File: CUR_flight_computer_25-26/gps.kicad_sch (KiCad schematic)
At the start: 4 parts, among them U1 SAM-M8Q

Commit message: update gps
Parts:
- removed C13: 1u, symbol Device:C_Small
- added 10k: R_Small_US, symbol Device:R_Small_US
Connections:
- net +3V3: now also 10k.2
- net ~{GPS_RES}: now also 10k.1
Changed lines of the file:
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@@
 	)
 	(junction
-		(at 149.86 86.36)
+		(at 120.65 114.3)
 		(diameter 0)
 		(color 0 0 0 0)
@@
 	(wire
 		(pts
-			(xy 142.24 86.36) (xy 149.86 86.36)
-		)
-		(stroke
-			(width 0)
-			(type default)
-		)
-	)
-	(wire
-		(pts
 			(xy 165.1 106.68) (xy 167.64 106.68)
 		)
@@
 	(wire
 		(pts
-			(xy 142.24 87.63) (xy 142.24 86.36)
-		)
-		(stroke
-			(width 0)
-			(type default)
-		)
-	)
-	(wire
-		(pts
 			(xy 172.72 104.14) (xy 177.8 104.14)
 		)
@@
 	(wire
 		(pts
+			(xy 120.65 102.87) (xy 120.65 105.41)
+		)
+		(stroke
+			(width 0)
+			(type default)
+		)
+	)
+	(wire
+		(pts
 			(xy 152.4 96.52) (xy 152.4 92.71)
 		)
@@
 	(wire
 		(pts
-			(xy 135.89 114.3) (xy 139.7 114.3)
+			(xy 116.84 114.3) (xy 120.65 114.3)
 		)
 		(stroke
@@
 	(wire
 		(pts
-			(xy 149.86 86.36) (xy 149.86 92.71)
-		)
-		(stroke
-			(width 0)
-			(type default)
-		)
-	)
-	(wire
-		(pts
 			(xy 172.72 106.68) (xy 177.8 106.68)
 		)
@@
 	(wire
 		(pts
+			(xy 120.65 114.3) (xy 139.7 114.3)
+		)
+		(stroke
+			(width 0)
+			(type default)
+		)
+	)
+	(wire
+		(pts
+			(xy 120.65 110.49) (xy 120.65 114.3)
+		)
+		(stroke
+			(width 0)
+			(type default)
+		)
+	)
+	(wire
+		(pts
 			(xy 152.4 92.71) (xy 149.86 92.71)
 		)
@@
 	(wire
 		(pts
-			(xy 149.86 83.82) (xy 149.86 86.36)
+			(xy 149.86 83.82) (xy 149.86 92.71)
 		)
 		(stroke
@@
 	(hierarchical_label "~{GPS_RES}"
 		(shape input)
-		(at 135.89 114.3 180)
+		(at 116.84 114.3 180)
 		(effects
 			(font
@@
 	)
 	(hierarchical_label "GPS_EXINT"
-		(shape input)
+		(shape output)
 		(at 135.89 106.68 180)
 		(effects
@@
 			)
 			(justify left)
+		)
+	)
+	(symbol
+		(lib_id "power:+3V3")
+		(at 120.65 102.87 0)
+		(unit 1)
+		(exclude_from_sim no)
+		(in_bom yes)
+		(on_board yes)
+		(dnp no)
+		(fields_autoplaced yes)
+		(property "Reference" "#PWR034"
+			(at 120.65 106.68 0)
+			(effects
+				(font
+					(size 1.27 1.27)
+				)
+				(hide yes)
+			)
+		)
+		(property "Value" "+3V3"
+			(at 120.65 97.79 0)
+			(effects
+				(font
+					(size 1.27 1.27)
+				)
+			)
+		)
+		(property "Footprint" ""
+			(at 120.65 102.87 0)
+			(effects
+				(font
+					(size 1.27 1.27)
+				)
+				(hide yes)
+			)
+		)
+		(property "Datasheet" ""
+			(at 120.65 102.87 0)
+			(effects
+				(font
+					(size 1.27 1.27)
+				)
+				(hide yes)
+			)
+		)
+		(property "Description" "Power symbol creates a global label with name \"+3V3\""
+			(at 120.65 102.87 0)
+			(effects
+				(font
+					(size 1.27 1.27)
+				)
+				(hide yes)
+			)
+		)
+		(pin "1"
+		)
+		(instances
+			(project ""
+				(path "/bf7761cc-1b32-4d86-809c-5f027005229b/e838d24c-cb75-4a46-b88f-e4466a269629"
+					(reference "#PWR034")
+					(unit 1)
+				)
+			)
 		)
 	)
@@
 	)
 	(symbol
-		(lib_id "power:GND")
-		(at 142.24 92.71 0)
-		(unit 1)
-		(exclude_from_sim no)
-		(in_bom yes)
-		(on_board yes)
-		(dnp no)
-		(fields_autoplaced yes)
-		(property "Reference" "#PWR013"
-			(at 142.24 99.06 0)
-			(effects
-				(font
-					(size 1.27 1.27)
-				)
-				(hide yes)
-			)
-		)
-		(property "Value" "GND"
-			(at 142.24 97.79 0)
-			(effects
-				(font
-					(size 1.27 1.27)
-				)
-			)
-		)
-		(property "Footprint" ""
-			(at 142.24 92.71 0)
-			(effects
-				(font
-					(size 1.27 1.27)
-				)
-				(hide yes)
-			)
-		)
-		(property "Datasheet" ""
-			(at 142.24 92.71 0)
-			(effects
-				(font
-					(size 1.27 1.27)
-				)
-				(hide yes)
-			)
-		)
-		(property "Description" "Power symbol creates a global label with name \"GND\" , ground"
-			(at 142.24 92.71 0)
-			(effects
-				(font
-					(size 1.27 1.27)
-				)
-				(hide yes)
-			)
-		)
-		(pin "1"
-		)
-		(instances
-			(project ""
-				(path "/bf7761cc-1b32-4d86-809c-5f027005229b/e838d24c-cb75-4a46-b88f-e4466a269629"
-					(reference "#PWR013")
-					(unit 1)
-				)
-			)
-		)
-	)
-	(symbol
 		(lib_id "Device:R_Small")
 		(at 170.18 104.14 90)
@@
 	)
 	(symbol
-		(lib_id "Device:C_Small")
-		(at 142.24 90.17 0)
-		(unit 1)
-		(exclude_from_sim no)
-		(in_bom yes)
-		(on_board yes)
-		(dnp no)
-		(fields_autoplaced yes)
-		(property "Reference" "C13"
-			(at 144.78 88.9062 0)
-			(effects
-				(font
-					(size 1.27 1.27)
-				)
-				(justify left)
-			)
-		)
-		(property "Value" "1u"
-			(at 144.78 91.4462 0)
-			(effects
-				(font
-					(size 1.27 1.27)
-				)
-				(justify left)
-			)
-		)
-		(property "Footprint" ""
-			(at 142.24 90.17 0)
-			(effects
-				(font
-					(size 1.27 1.27)
-				)
-				(hide yes)
-			)
-		)
-		(property "Datasheet" "~"
-			(at 142.24 90.17 0)
-			(effects
-				(font
-					(size 1.27 1.27)
-				)
-				(hide yes)
-			)
-		)
-		(property "Description" "Unpolarized capacitor, small symbol"
-			(at 142.24 90.17 0)
-			(effects
-				(font
-					(size 1.27 1.27)
-				)
-				(hide yes)
-			)
-		)
-		(pin "2"
-		)
-		(pin "1"
-		)
-		(instances
-			(project ""
-				(path "/bf7761cc-1b32-4d86-809c-5f027005229b/e838d24c-cb75-4a46-b88f-e4466a269629"
-					(reference "C13")
-					(unit 1)
-				)
-			)
-		)
-	)
-	(symbol
 		(lib_id "Device:R_Small")
 		(at 170.18 106.68 90)
@@
 					(unit 1)
 				)
+			)
+		)
+	)
+	(symbol
+		(lib_id "Device:R_Small_US")
+		(at 120.65 107.95 0)
+		(mirror x)
+		(unit 1)
+		(exclude_from_sim no)
+		(in_bom yes)
+		(on_board yes)
+		(dnp no)
+		(fields_autoplaced yes)
+		(property "Reference" "10k"
+			(at 118.11 106.6799 0)
+			(effects
+				(font
+					(size 1.27 1.27)
+				)
+				(justify right)
+			)
+		)
+		(property "Value" "R_Small_US"
+			(at 118.11 109.2199 0)
+			(effects
+				(font
+					(size 1.27 1.27)
+				)
+				(justify right)
+			)
+		)
+		(property "Footprint" ""
+			(at 120.65 107.95 0)
+			(effects
+				(font
+					(size 1.27 1.27)
+				)
+				(hide yes)
+			)
+		)
+		(property "Datasheet" "~"
+			(at 120.65 107.95 0)
+			(effects
+				(font
+					(size 1.27 1.27)
+				)
+				(hide yes)
+			)
+		)
+		(property "Description" "Resistor, small US symbol"
+			(at 120.65 107.95 0)
+			(effects
+				(font
+					(size 1.27 1.27)
+				)
+				(hide yes)
+			)
+		)
+		(pin "1"
+		)
+		(pin "2"
+		)
+		(instances
+			(project ""
+				(path "/bf7761cc-1b32-4d86-809c-5f027005229b/e838d24c-cb75-4a46-b88f-e4466a269629"
+					(reference "10k")
+					(unit 1)
+				)

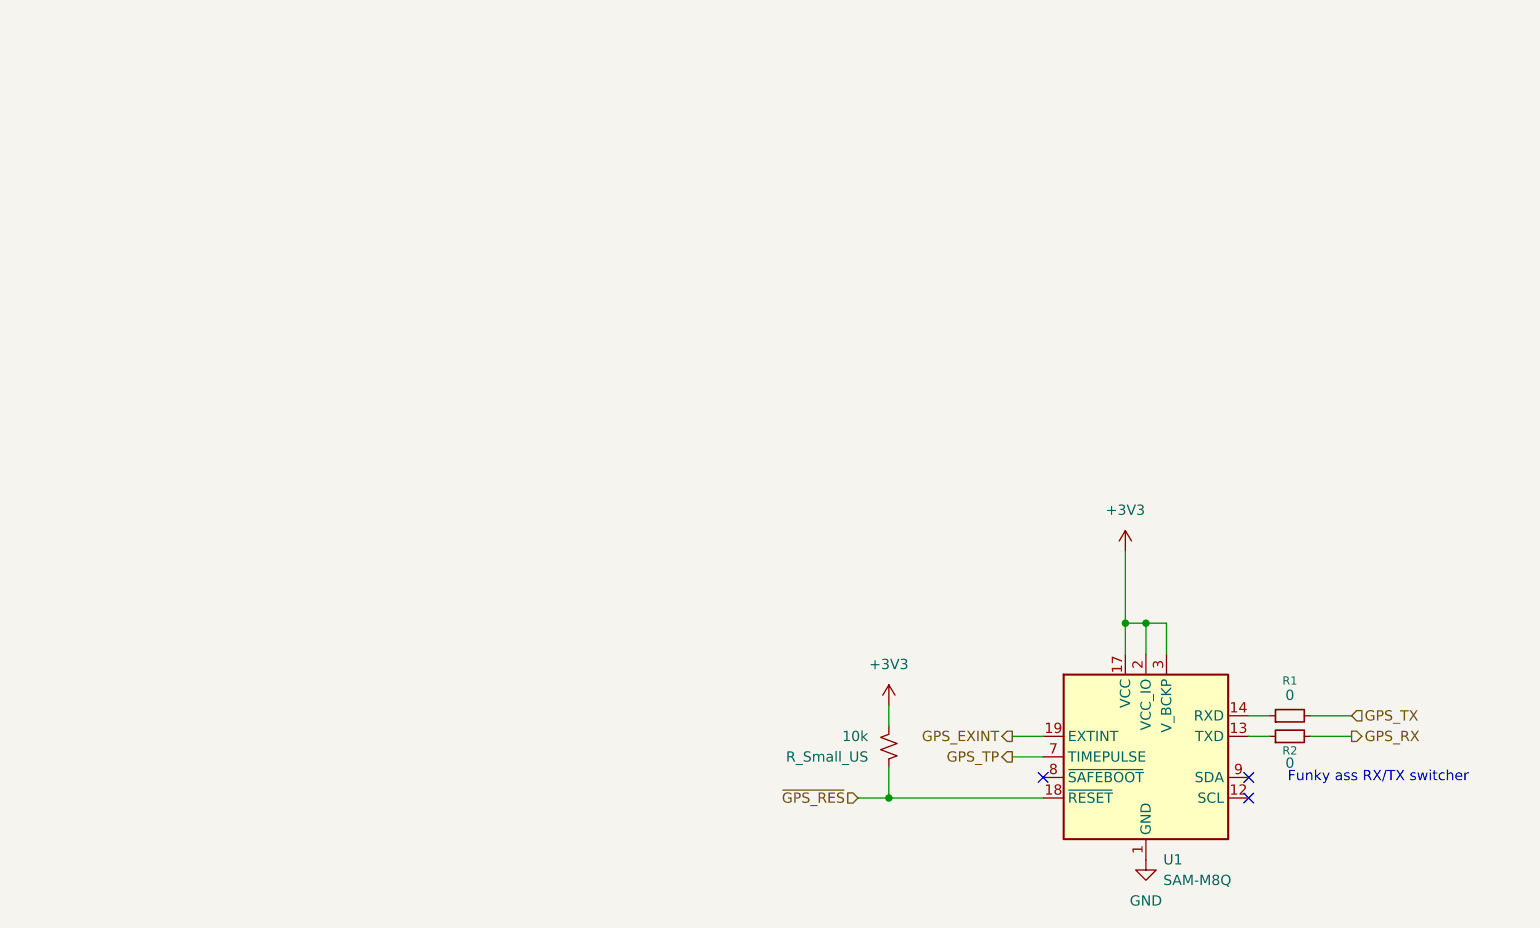
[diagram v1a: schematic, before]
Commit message: MCU work
added decoupling, reset button

need to figure out vddusb
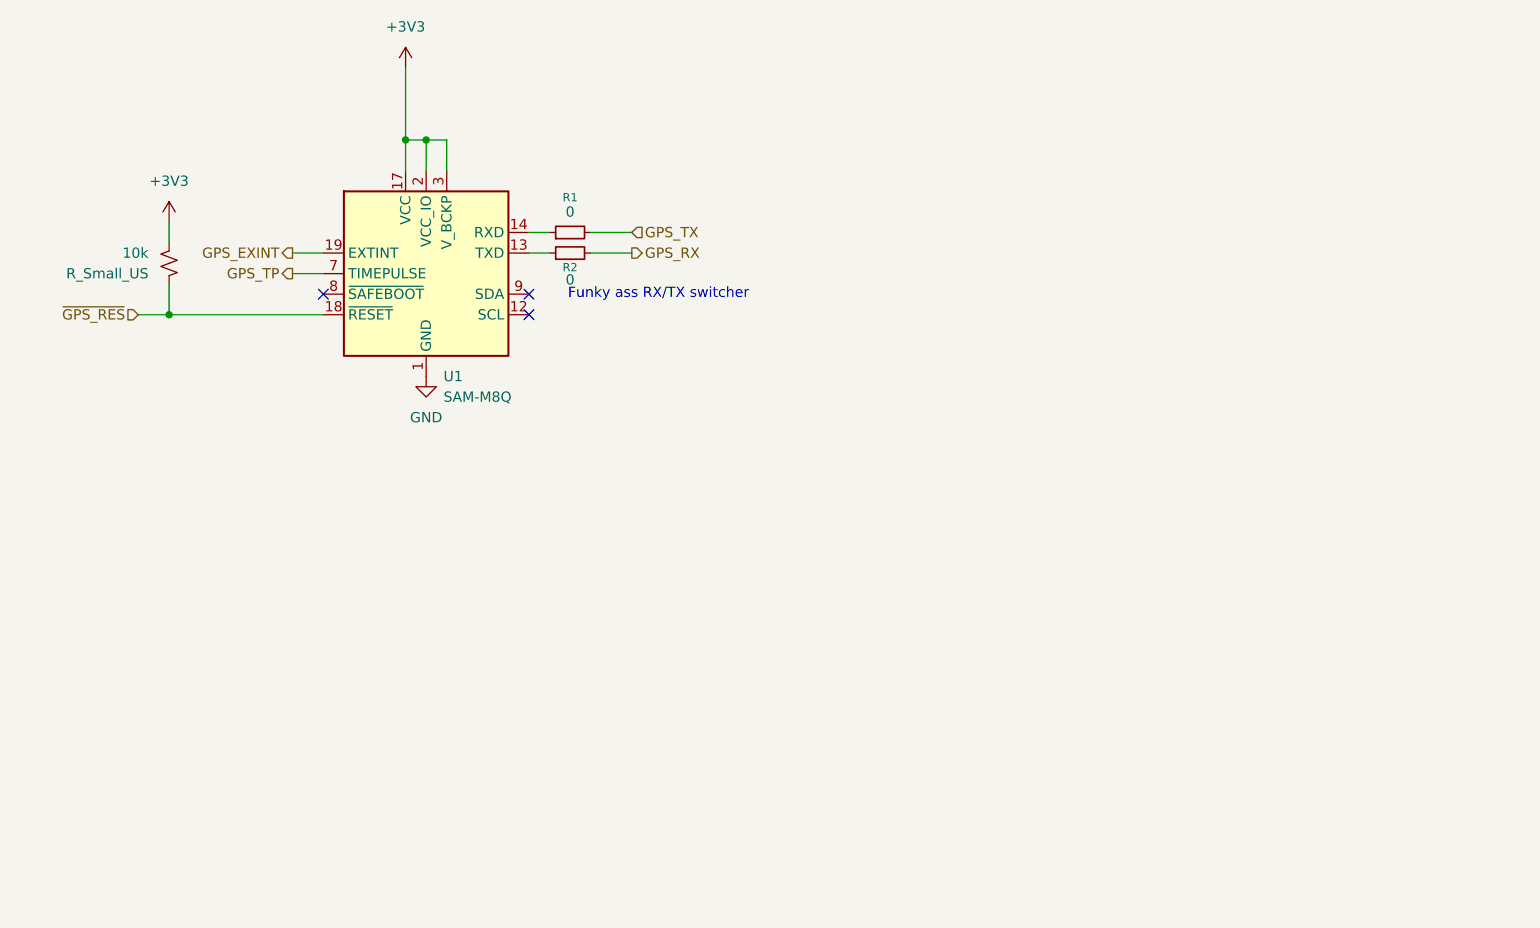
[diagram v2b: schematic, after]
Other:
- moved on the sheet: 10k, R1, R2, U1

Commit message: Implement RF reference design for LoRA module
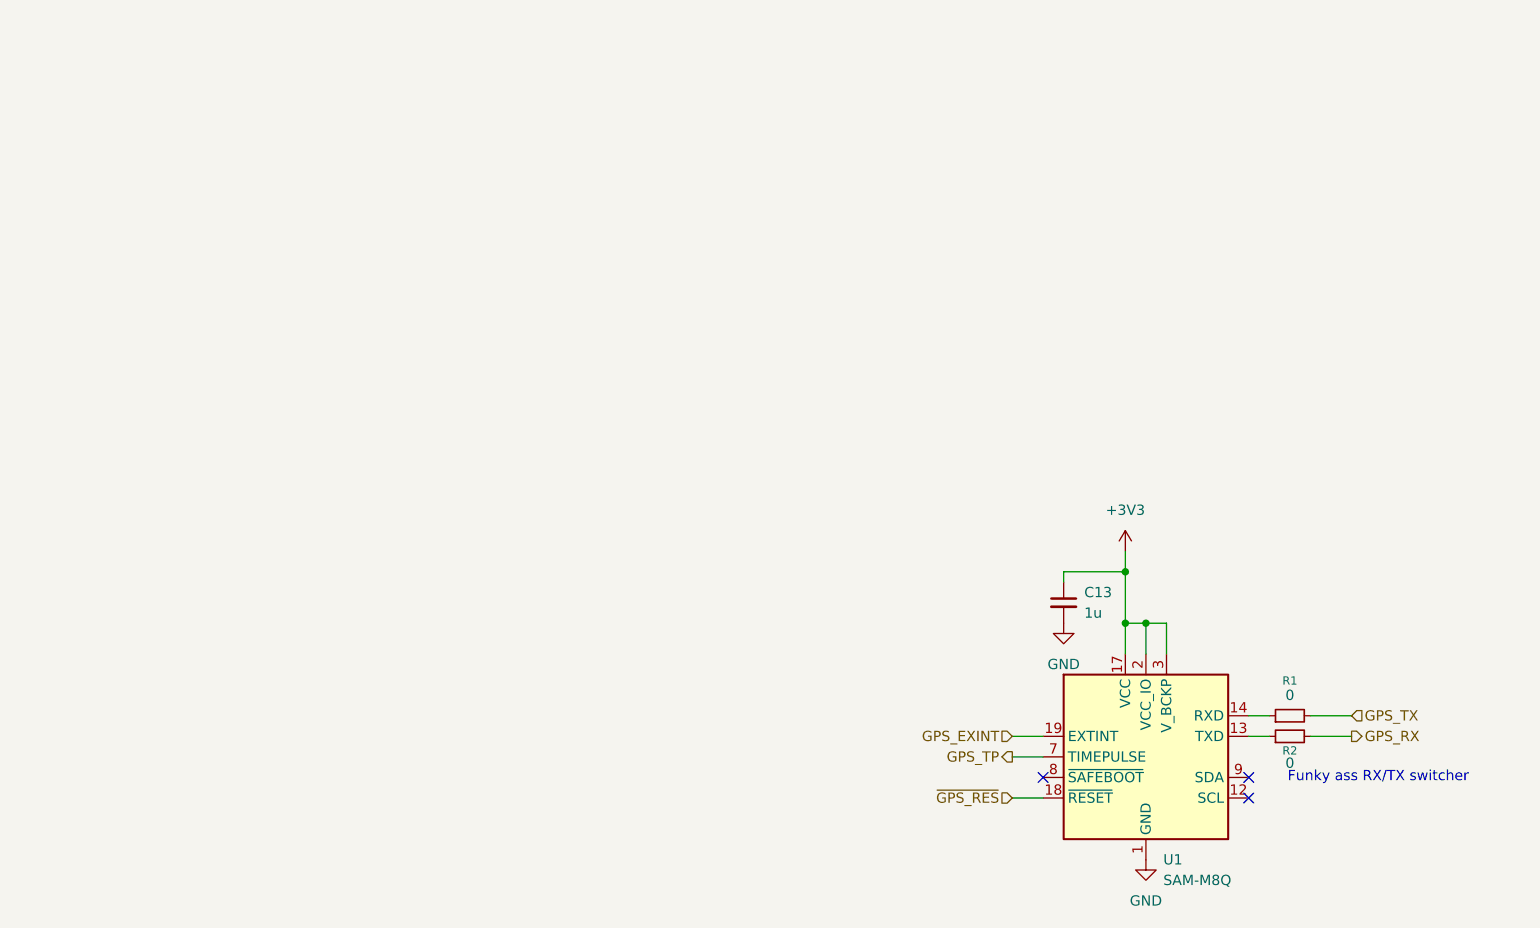
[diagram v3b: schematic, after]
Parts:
- removed 10k: R_Small_US, symbol Device:R_Small_US
- added C13: 1u, symbol Device:C_Small
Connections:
- net +3V3: now also C13.1
- net GND: now also C13.2
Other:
- moved on the sheet: R1, R2, U1

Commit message: edited gps
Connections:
- net ~{GPS_RES} renamed ~{GPS_RESET}
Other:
- note added: "Leave as 0 for now can be used for emi protection (R>20), ferrite beads, inductors but may affect signal timing"
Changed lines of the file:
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@@
 	(generator_version "9.0")
 	(paper "A4")
+	(text "Leave as 0 for now\ncan be used for emi protection\n(R>20), ferrite beads, inductors\nbut may affect signal timing"
+		(exclude_from_sim no)
+		(at 179.578 92.964 0)
+		(effects
+			(font
+				(size 1.27 1.27)
+			)
+		)
+	)
 	(text "Funky ass RX/TX switcher"
 		(exclude_from_sim no)
@@
 		)
 	)
-	(hierarchical_label "~{GPS_RES}"
+	(hierarchical_label "~{GPS_RESET}"
 		(shape input)
 		(at 135.89 114.3 180)
